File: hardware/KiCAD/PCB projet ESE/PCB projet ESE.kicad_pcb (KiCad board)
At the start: 4 copper layers, 53 x 46 mm, 82 parts, among them J1 Conn_01x06, J10 Conn_01x06, J11 Conn_01x06, J12 Conn_01x06, J13 Conn_01x06, J14 Conn_01x06, J15 Conn_01x06, J16 Conn_01x04, J2 Conn_01x04, J3 Conn_01x06, J4 Conn_01x03, J7 Conn_01x04, J8 Conn_01x02, J9 Conn_ST_STDC14, SW1 SW_SPST, SW2 472121010111, U1 ZXBM5210-SP, U2 ZXBM5210-SP, U3 STM32G474RETx, U4 ADXL343

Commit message: BOM
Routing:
- added copper zone on B.Cu, net +7.4V
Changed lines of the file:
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@@
+	)
+	(zone
+		(net 54)
+		(net_name "+7.4V")
+		(layer "B.Cu")
+		(hatch edge 0.5)
+		(priority 6)
+		(connect_pads
+			(clearance 0.5)
+		)
+		(min_thickness 0.25)
+		(filled_areas_thickness no)
+		(fill yes
+			(thermal_gap 0.5)
+			(thermal_bridge_width 0.5)
+			(smoothing fillet)
+			(radius 1)
+		)
+		(polygon
+			(pts
+				(xy 89.9 80.9) (xy 89.8 80) (xy 89.2 80) (xy 89.2 77.9) (xy 90.5 77.9) (xy 90.7 80) (xy 90.9 80)
+				(xy 90.9 80.9)
+			)
+		)
 	)
 	(zone
@@
 			)
 		)
+	)
+	(zone
+		(net 54)
+		(net_name "+7.4V")
+		(layer "B.Cu")
+		(hatch edge 0.5)
+		(priority 5)
+		(connect_pads
+			(clearance 0.5)
+		)
+		(min_thickness 0.25)
+		(filled_areas_thickness no)
+		(fill yes
+			(thermal_gap 0.5)
+			(thermal_bridge_width 0.5)
+			(smoothing fillet)
+			(radius 1)
+		)
+		(polygon
+			(pts
+				(xy 88.05 71.1) (xy 88.05 74.9) (xy 90.5 74.9) (xy 90.4 71.1)
+			)
+		)

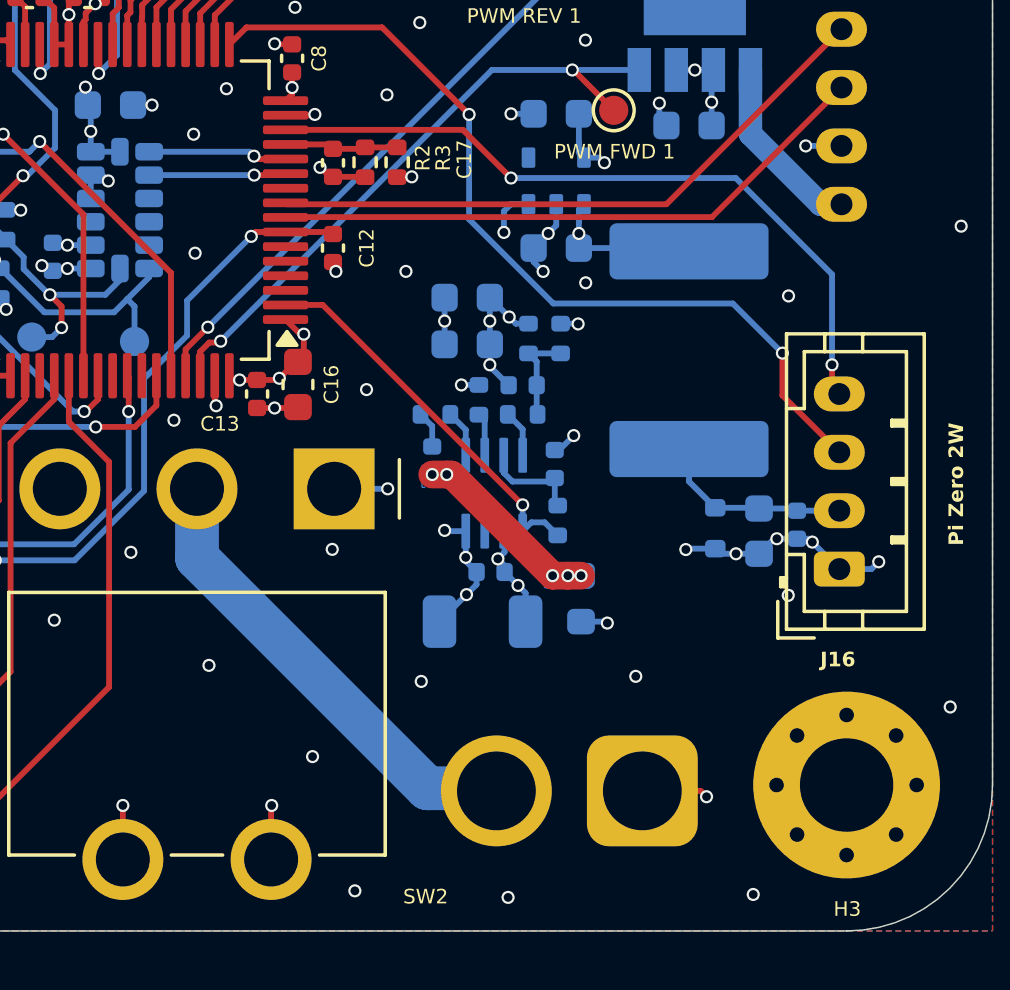
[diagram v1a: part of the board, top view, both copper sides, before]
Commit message: maj inductance 4.7uH
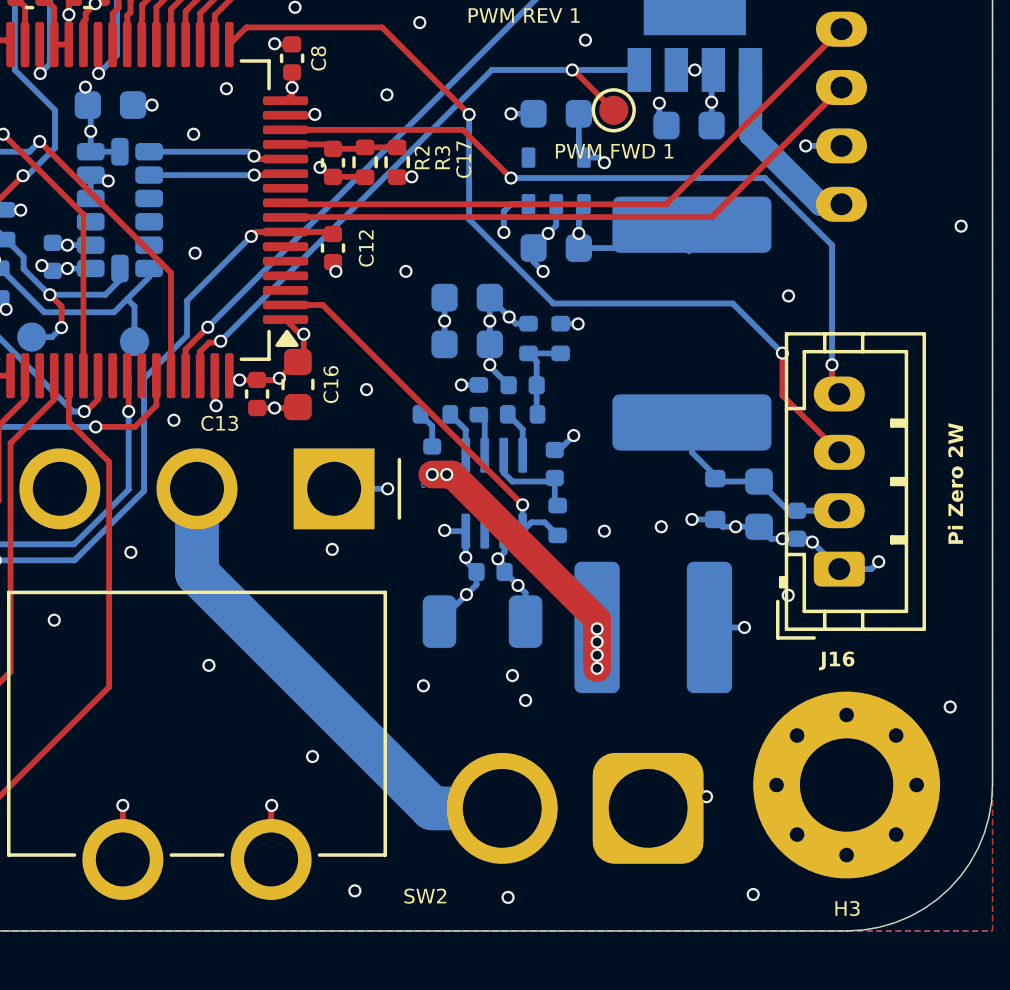
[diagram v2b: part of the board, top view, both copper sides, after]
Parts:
- C19, C21, C22, C23: value 0.1u -> 100n
- C3, C4: value 4.7u -> 4u7
- L2: value 4.7u -> 4u7; footprint Inductor_SMD:L_0603_1608Metric -> Régu:74404054068
- R14: value 7.68k -> 7k68
- R15: value 40.2k -> 40k2
- R2: value 18k -> 20k
- R3: value 10k -> 5k6
- moved L2 1.13 mm to (118.5, 89.6), turned to 0 degrees
- moved D5 1.00 mm to (122.5, 85.2)
- moved C30 0.92 mm to (124.0, 85.4)
- moved F2 0.92 mm to (121.7, 79.2)
- moved J8 0.63 mm to (120.2, 95.8)
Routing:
- net Net-(MP1-SW): track 9.43 -> 12.3 mm, vias 5 -> 6
- net Net-(J8-Pin_2): track 16.0 -> 16.7 mm
- net UART_Pi_Zero_TX: track 25.0 -> 25.6 mm
- net GND: track 85.9 -> 85.7 mm, vias 116 -> 118

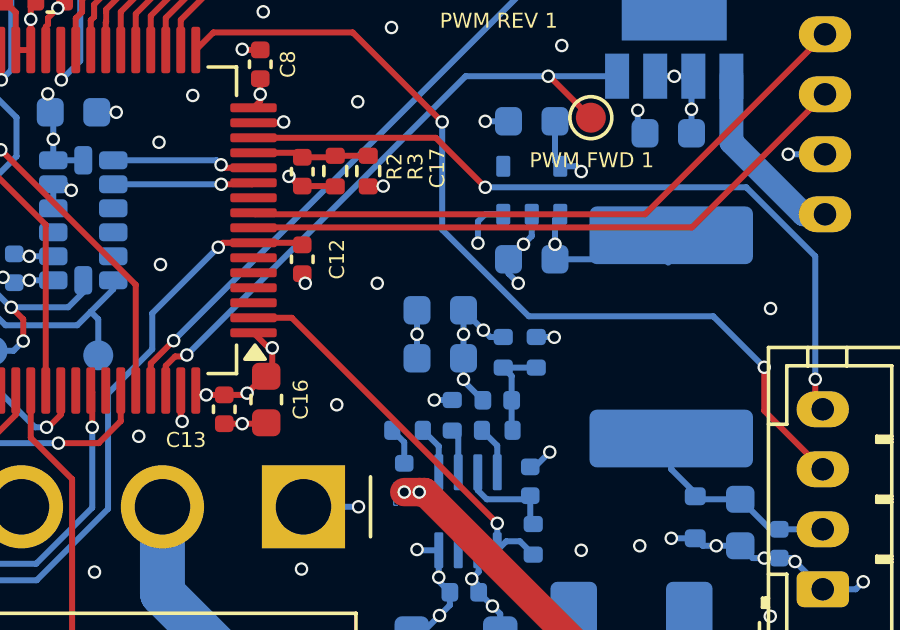
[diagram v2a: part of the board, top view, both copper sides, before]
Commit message: maj C25 & C26
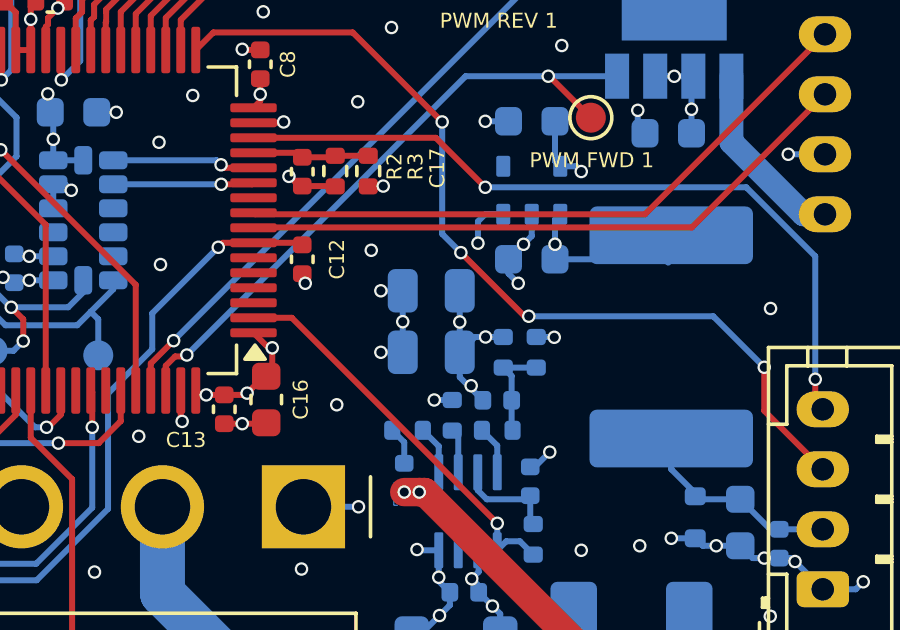
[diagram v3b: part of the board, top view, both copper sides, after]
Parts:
- C25, C26: footprint Capacitor_SMD:C_0603_1608Metric -> Capacitor_SMD:C_0805_2012Metric
- moved C26 0.72 mm to (113.7, 77.7)
- moved C25 0.36 mm to (113.7, 79.7)
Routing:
- net GND: track 85.7 -> 87.6 mm, vias 118 -> 120
- net +5V: track 16.7 -> 17.4 mm
- net UART_Pi_Zero_RX: track 30.1 -> 30.2 mm, vias 2 -> 4
